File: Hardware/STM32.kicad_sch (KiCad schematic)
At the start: 38 parts, among them U2 STM32L4R5ZITx

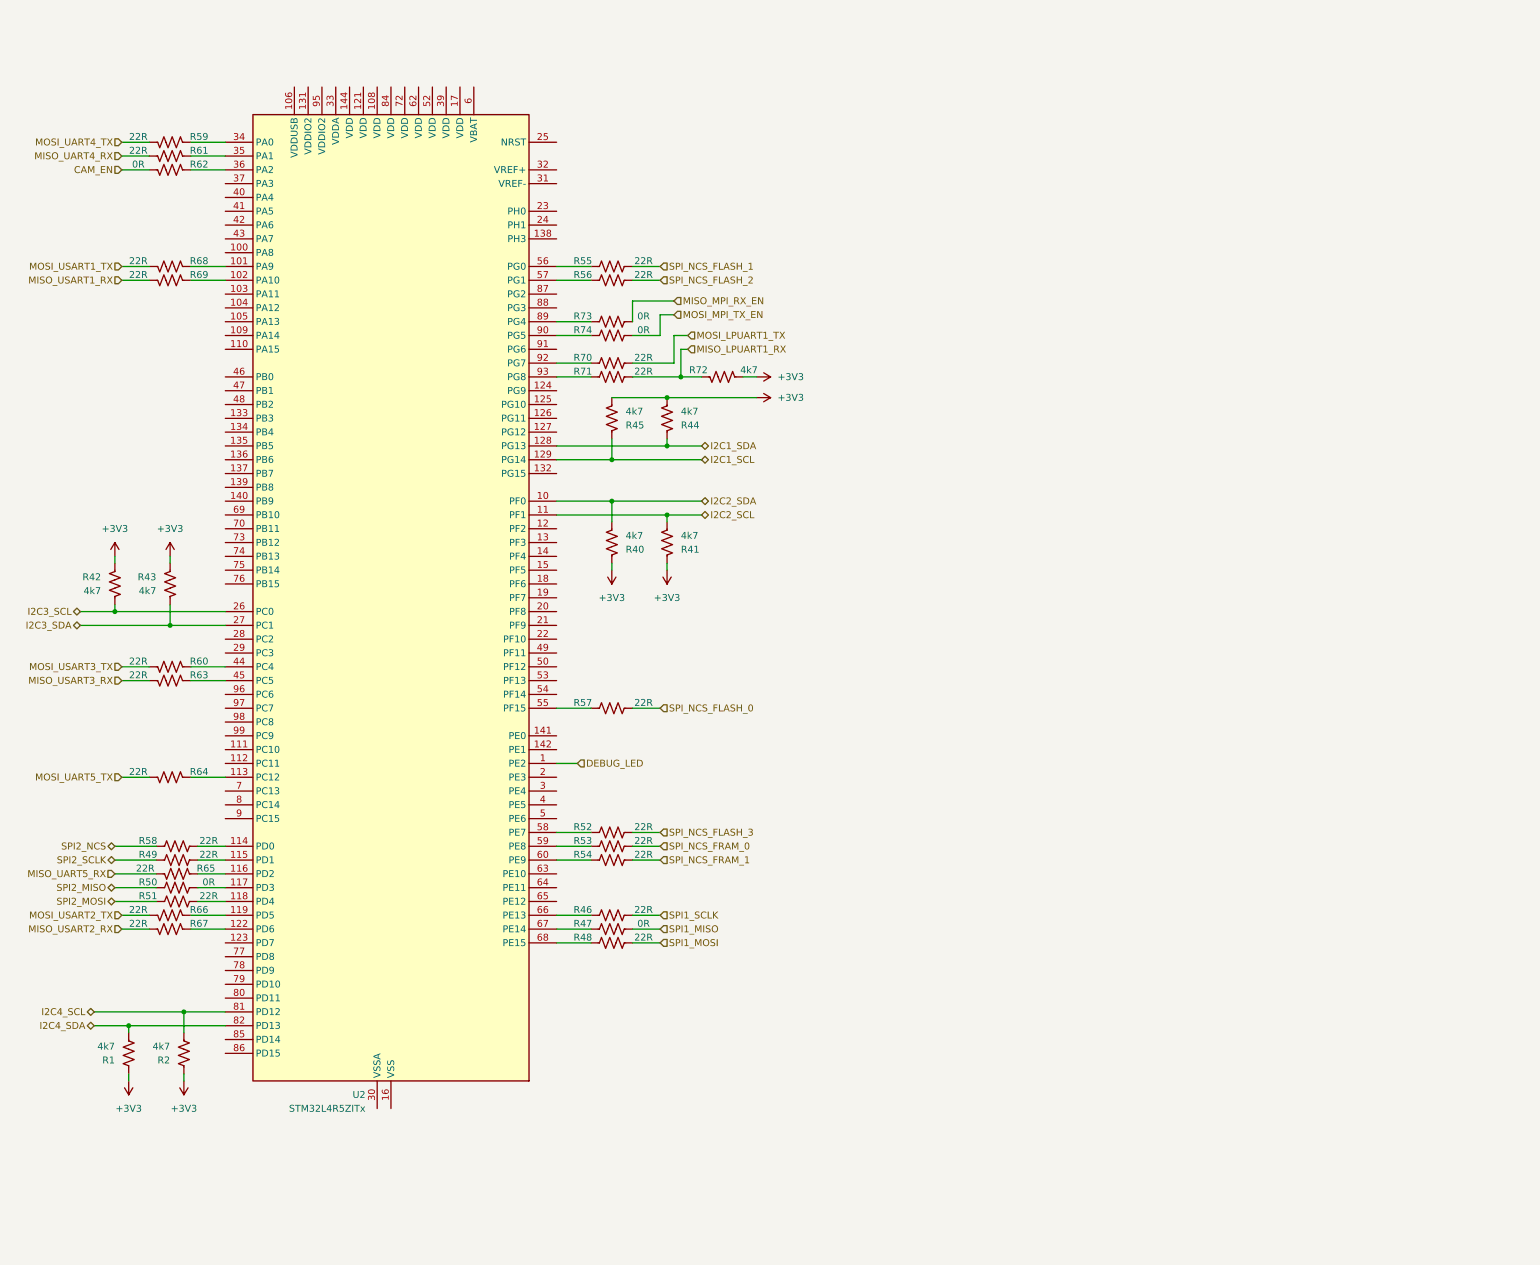
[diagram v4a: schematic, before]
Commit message: Add remaining STM32 connections
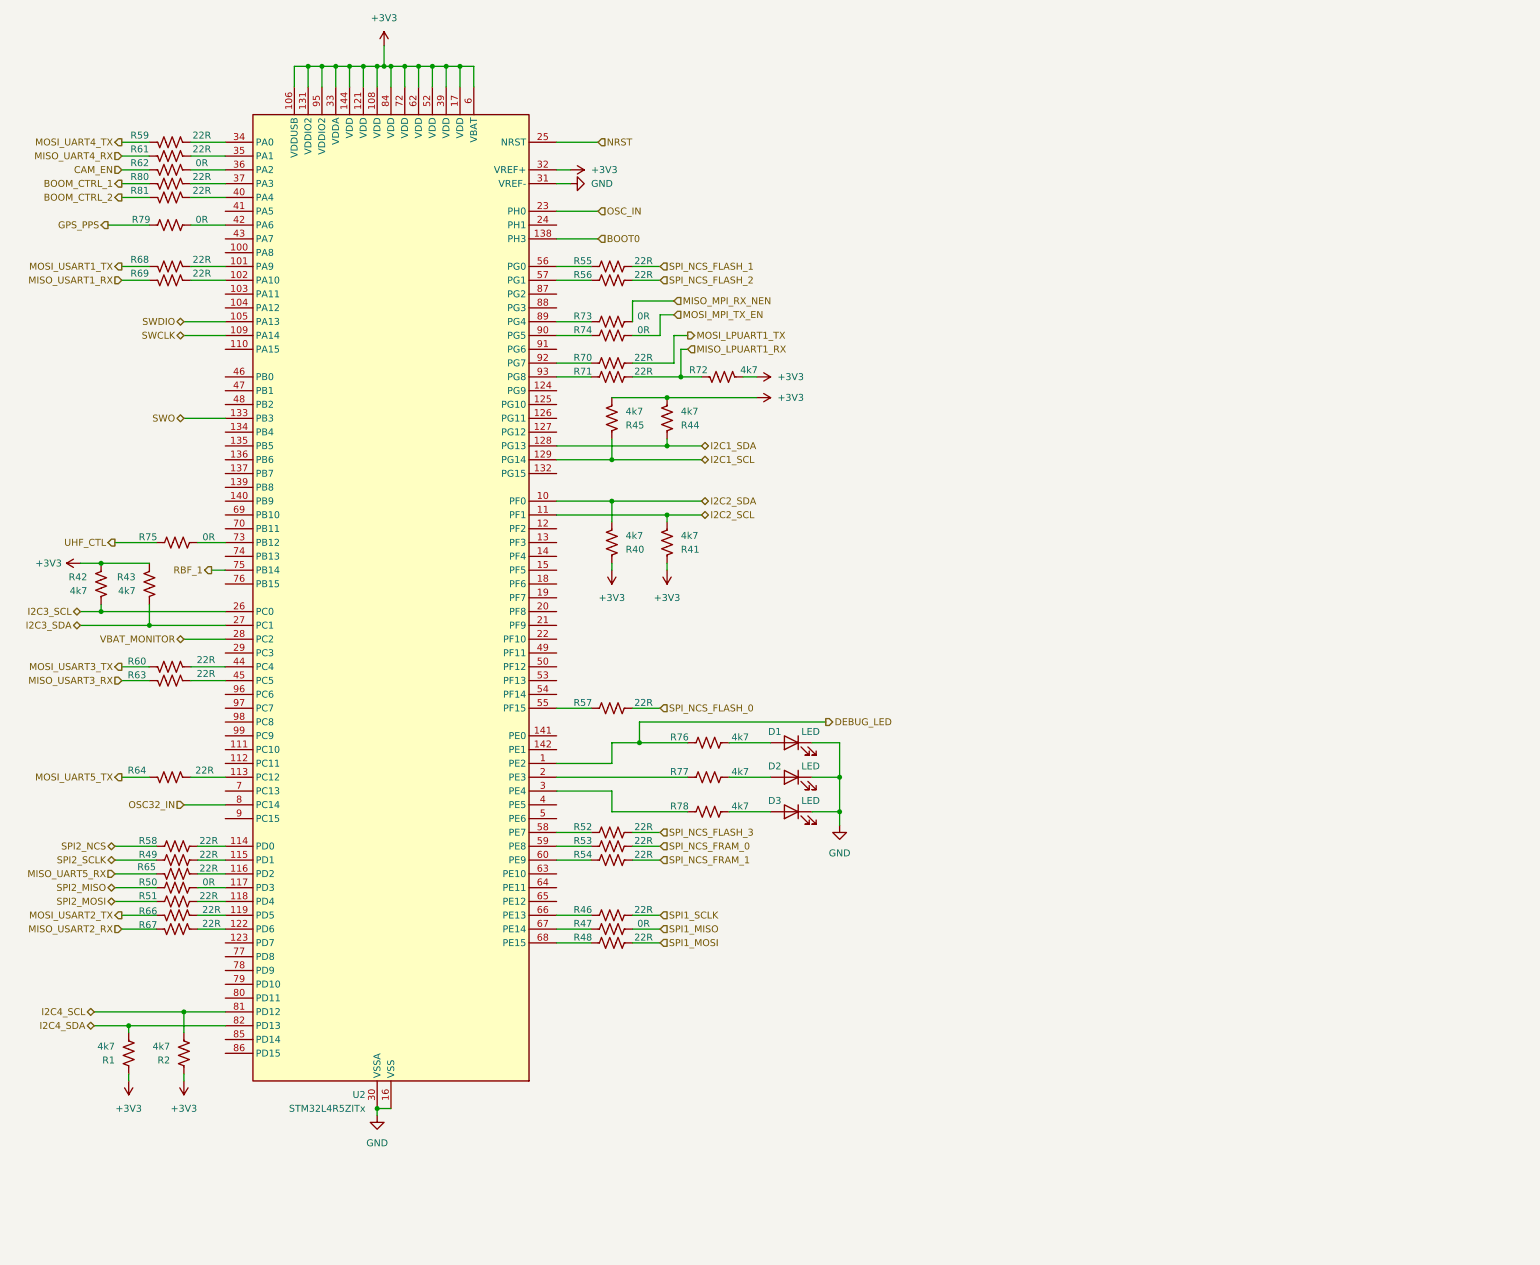
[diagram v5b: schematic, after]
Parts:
- added D1, D2, D3: LED, symbol Device:LED
- added R75, R79: 0R, symbol Device:R_US
- added R76, R77, R78: 4k7, symbol Device:R_US
- added R80, R81: 22R, symbol Device:R_US
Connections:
- net +3V3: now also U2.106 (VDDUSB), U2.108 (VDD), U2.121 (VDD), U2.131 (VDDIO2), U2.144 (VDD), U2.17 (VDD), U2.32 (VREF+), U2.33 (VDDA), U2.39 (VDD), U2.52 (VDD), U2.6 (VBAT), U2.62 (VDD), U2.72 (VDD), U2.84 (VDD), U2.95 (VDDIO2)
- net DEBUG_LED: now also R76.1
- net SWDIO: now reaches U2.105 (PA13)
- net GND: now reaches U2.107 (VSS), U2.120 (VSS), U2.130 (VSS), U2.143 (VSS), U2.16 (VSS), U2.38 (VSS), U2.51 (VSS), U2.61 (VSS), U2.71 (VSS), U2.83 (VSS), U2.94 (VSS)
- net GND: now also U2.30 (VSSA), U2.31 (VREF-), D1.1 (K), D2.1 (K), D3.1 (K)
- net SWCLK: now reaches U2.109 (PA14)
- net SWO: now reaches U2.133 (PB3)
- net BOOT0: now reaches U2.138 (PH3)
- net at U2.2 (PE3): now also R77.1
- net OSC_IN: now reaches U2.23 (PH0)
- net NRST: now reaches U2.25 (NRST)
- net VBAT_MONITOR: now reaches U2.28 (PC2)
- net at U2.3 (PE4): now also R78.1
- net at U2.37 (PA3): now also R80.1
- net at U2.40 (PA4): now also R81.1
- net at U2.42 (PA6): now also R79.2
- net at U2.73 (PB12): now also R75.2
- net RBF_1: now reaches U2.75 (PB14)
- net OSC32_IN: now reaches U2.8 (PC14)
- net MISO_MPI_RX_EN renamed MISO_MPI_RX_NEN
- new net: D2.2 (A), R77.2
- new net: D1.2 (A), R76.2
- new net: D3.2 (A), R78.2
- new net BOOM_CTRL_1: R80.2
- new net BOOM_CTRL_2: R81.2
- new net GPS_PPS: R79.1
- new net UHF_CTL: R75.1
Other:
- moved on the sheet: R42, R43, R66, R67

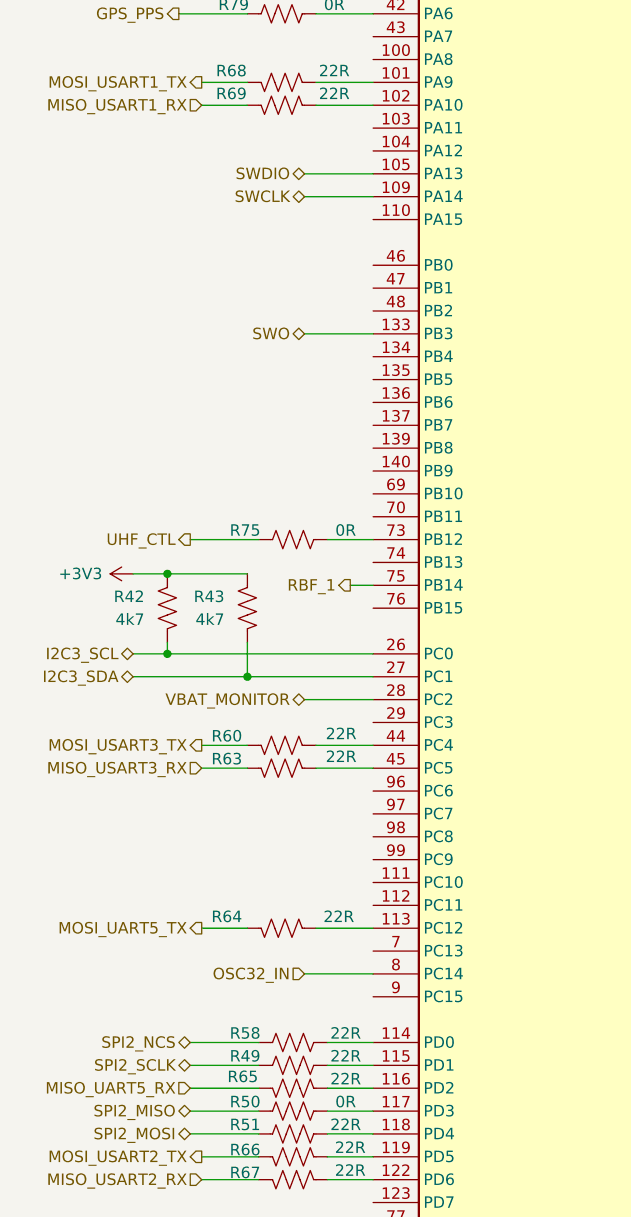
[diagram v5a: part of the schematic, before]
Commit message: Assign SPI1 to Pi 4 <--> STM32
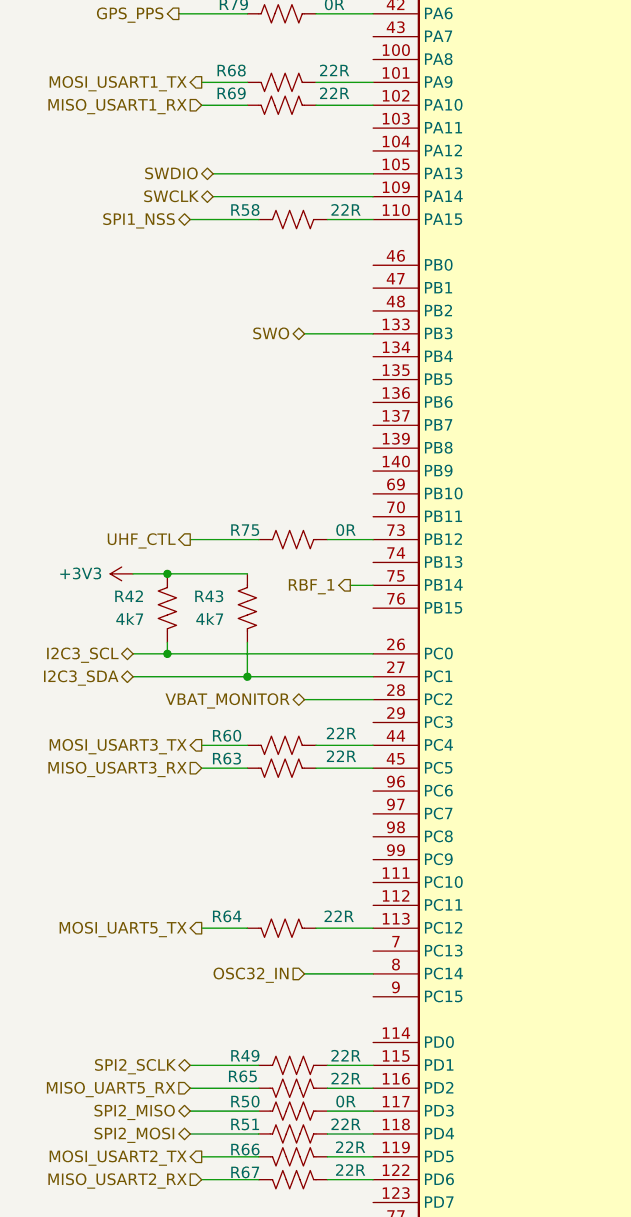
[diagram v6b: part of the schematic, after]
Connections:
- net at R58.2: now also U2.110 (PA15); no longer U2.114 (PD0)
- net SPI2_NCS renamed SPI1_NSS
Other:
- moved on the sheet: R58
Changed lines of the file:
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@@
 	(wire
 		(pts
-			(xy 54.61 76.2) (xy 62.23 76.2)
+			(xy 44.45 76.2) (xy 62.23 76.2)
 		)
 		(stroke
@@
 	(wire
 		(pts
+			(xy 57.15 78.74) (xy 62.23 78.74)
+		)
+		(stroke
+			(width 0)
+			(type default)
+		)
+	)
+	(wire
+		(pts
 			(xy 149.86 99.06) (xy 133.35 99.06)
 		)
@@
 	(wire
 		(pts
-			(xy 41.91 170.18) (xy 49.53 170.18)
+			(xy 41.91 78.74) (xy 49.53 78.74)
 		)
 		(stroke
@@
 	(wire
 		(pts
-			(xy 57.15 170.18) (xy 62.23 170.18)
-		)
-		(stroke
-			(width 0)
-			(type default)
-		)
-	)
-	(wire
-		(pts
 			(xy 175.26 157.48) (xy 175.26 163.83)
 		)
@@
 	(wire
 		(pts
-			(xy 54.61 73.66) (xy 62.23 73.66)
+			(xy 44.45 73.66) (xy 62.23 73.66)
 		)
 		(stroke
@@
 		)
 	)
-	(hierarchical_label "I2C2_SCL"
+	(hierarchical_label "SPI1_NSS"
 		(shape bidirectional)
-		(at 149.86 109.22 0)
+		(at 41.91 78.74 180)
 		(effects
 			(font
 				(size 1.27 1.27)
 			)
-			(justify left)
+			(justify right)
 		)
 	)
-	(hierarchical_label "MISO_UART4_RX"
-		(shape input)
-		(at 43.18 43.18 180)
+	(hierarchical_label "I2C2_SCL"
+		(shape bidirectional)
+		(at 149.86 109.22 0)
 		(effects
 			(font
 				(size 1.27 1.27)
 			)
-			(justify right)
+			(justify left)
 		)
 	)
-	(hierarchical_label "SPI2_NCS"
-		(shape bidirectional)
-		(at 41.91 170.18 180)
+	(hierarchical_label "MISO_UART4_RX"
+		(shape input)
+		(at 43.18 43.18 180)
 		(effects
 			(font
@@
 	(hierarchical_label "SWDIO"
 		(shape bidirectional)
-		(at 54.61 73.66 180)
+		(at 44.45 73.66 180)
 		(effects
 			(font
@@
 	(hierarchical_label "SWCLK"
 		(shape bidirectional)
-		(at 54.61 76.2 180)
+		(at 44.45 76.2 180)
 		(effects
 			(font
@@
 	(symbol
 		(lib_id "Device:R_US")
-		(at 53.34 170.18 90)
+		(at 53.34 78.74 90)
 		(unit 1)
 		(exclude_from_sim no)
@@
 		(dnp no)
 		(property "Reference" "R58"
-			(at 48.006 169.164 90)
+			(at 48.006 77.724 90)
 			(effects
 				(font
@@
 		)
 		(property "Value" "22R"
-			(at 59.182 169.164 90)
+			(at 59.182 77.724 90)
 			(effects
 				(font
@@
 		)
 		(property "Footprint" ""
-			(at 53.594 169.164 90)
+			(at 53.594 77.724 90)
 			(effects
 				(font
@@
 		)
 		(property "Datasheet" "~"
-			(at 53.34 170.18 0)
+			(at 53.34 78.74 0)
 			(effects
 				(font
@@
 		)
 		(property "Description" "Resistor, US symbol"
-			(at 53.34 170.18 0)
+			(at 53.34 78.74 0)
 			(effects
 				(font

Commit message: Small updates
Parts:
- added IC1: STTS22HTR, SON65P200X200X55-7N-D, symbol STTS22HTR:STTS22HTR
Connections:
- net +3V3: now also IC1.3 (VDD)
- net GND: now also IC1.4 (ADDR), IC1.5 (GND)
- net I2C4_SCL: now also IC1.1 (SCL)
- net I2C4_SDA: now also IC1.6 (SDA)
- net DEBUG_LED: no longer names the net of R76.1, U2.1 (PE2)
- no-connect marks 0 -> 2
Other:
- moved on the sheet: D1, D2, D3, R1, R2, R40, R41, R42, R43, R44, R45, R46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

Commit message: RP2040 Schematic
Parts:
- renumbered R61 to R10, R62 to R11, R80 to R12, R81 to R13, R79 to R14, R68 to R15, R69 to R16, R60 to R17, R63 to R18, R64 to R19, R58 to R20, R75 to R21, R49 to R22, R65 to R23, R50 to R24, R51 to R25, R66 to R26, R67 to R27, R2 to R28, R55 to R29, R56 to R30, R73 to R31, R74 to R32, R70 to R33, R71 to R34, R45 to R35, R40 to R36, R57 to R37, R52 to R38, R53 to R39, R54 to R40, R46 to R41, R47 to R42, R48 to R43, R41 to R45, R76 to R46, R77 to R47, R78 to R48, R72 to R49, R42 to R6, R1 to R7, R43 to R8, R59 to R9, U2 to U3
